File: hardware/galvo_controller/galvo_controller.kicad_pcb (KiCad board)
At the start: 2 copper layers, 116 parts, among them J1 USB_OTG, J2 Conn_01x03, J3 Conn_01x03, J4 Micro_SD_Card_Det, J5 Red, J6 White, J7 Conn_01x03, J8 Conn_01x03, Q1 DDTD113ZC, Q2 MMBT2222, Q3 MMBT2222, U1 ESP-WROOM-32D, U2 CP2104, U3 TPS54295PWP, U4 PCM3060, U5 NCP1117LP, U6 OPA2134, U7 LME49724, U8 LME49724

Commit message: Working on component placement
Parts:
- added REF**: MountingHole_3.2mm_M3_Pad, Mounting_Holes:MountingHole_3.2mm_M3_Pad, F.Cu at (233.8, 137.0)
- added REF**: MountingHole_3.2mm_M3_Pad, Mounting_Holes:MountingHole_3.2mm_M3_Pad, F.Cu at (123.4, 137.8)
- added REF**: MountingHole_3.2mm_M3_Pad, Mounting_Holes:MountingHole_3.2mm_M3_Pad, F.Cu at (138.6, 39.2)
- added REF**: MountingHole_3.2mm_M3_Pad, Mounting_Holes:MountingHole_3.2mm_M3_Pad, F.Cu at (230.8, 50.0)
- moved J7 119.4 mm to (234.4, 104.9), turned to 90 degrees
- moved J4 114.5 mm to (202.4, 139.8), turned to 180 degrees
- moved J5 105.6 mm to (233.5, 65.5), turned to 270 degrees
- moved JP2 105.5 mm to (204.4, 162.2)
- moved J8 97.8 mm to (234.4, 124.5), turned to 90 degrees
- moved C13 96.2 mm to (177.1, 58.9)
- moved C25 92.5 mm to (209.8, 158.8)
- moved J6 91.6 mm to (233.5, 84.5), turned to 270 degrees
- moved C14 90.6 mm to (177.2, 61.8)
- moved C21 90.1 mm to (214.4, 56.4), turned to 180 degrees
- moved C39 85.8 mm to (227.6, 65.6), turned to 180 degrees
- moved U4 85.7 mm to (208.2, 106.4)
- moved C2 82.5 mm to (153.2, 134.0)
- moved C41 80.4 mm to (228.8, 81.0), turned to 270 degrees
- moved C16 78.6 mm to (199.8, 118.0)
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
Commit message: Working on component placement
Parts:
- moved L1 38.7 mm to (189.5, 51.2), turned to 90 degrees
- moved REF** 37.8 mm to (161.2, 137.2)
- moved R4 35.2 mm to (185.5, 58.2), turned to 90 degrees
- moved C12 35.1 mm to (190.3, 71.6), turned to 180 degrees
- moved R3 33.4 mm to (183.7, 58.2), turned to 270 degrees
- moved C8 33.3 mm to (189.9, 59.0), turned to 180 degrees
- moved C6 31.3 mm to (190.3, 57.0)
- moved R7 29.0 mm to (157.8, 172.8)
- moved C3 29.0 mm to (166.4, 165.8)
- moved R5 29.0 mm to (163.6, 175.8)
- moved R9 29.0 mm to (157.0, 155.4)
- moved C2 29.0 mm to (171.8, 156.2)
- moved D1 29.0 mm to (163.4, 172.2)
- moved D2 29.0 mm to (157.9, 176.7)
- moved Q2 29.0 mm to (163.5, 159.2)
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
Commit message: Working on component placement
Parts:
- moved C2 52.8 mm to (119.9, 146.7)
- moved C3 52.8 mm to (114.5, 156.3)
- moved D1 52.8 mm to (111.5, 162.7)
- moved Q2 52.8 mm to (111.6, 149.7)
- moved R7 52.8 mm to (105.9, 163.3)
- moved R9 52.8 mm to (105.1, 145.9)
- moved D2 52.8 mm to (106.0, 167.2)
- moved Q3 52.8 mm to (111.8, 142.6)
- moved R10 52.8 mm to (105.3, 150.5)
- moved R5 52.8 mm to (111.7, 166.3)
- moved C10 44.9 mm to (143.0, 76.0)
- moved C11 44.9 mm to (139.8, 71.8)
- moved C12 44.9 mm to (145.8, 77.2)
- moved C13 44.9 mm to (140.0, 84.4)
- moved C14 44.9 mm to (137.4, 84.4)
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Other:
- board outline added: 80 x 100 mm

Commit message: Working on component placement
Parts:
- moved R7 52.9 mm to (125.9, 114.3)
- moved R5 52.9 mm to (131.7, 117.3)
- moved D2 52.9 mm to (126.0, 118.2)
- moved D1 52.9 mm to (131.5, 113.7)
- moved C25 19.1 mm to (181.0, 151.4)
- moved JP2 19.1 mm to (175.6, 154.8)
- moved R14 19.1 mm to (158.8, 146.4)
- moved R15 19.1 mm to (160.4, 150.4)
- moved R16 19.1 mm to (160.8, 155.4)
- moved R17 19.1 mm to (169.4, 148.6)
- moved R19 19.1 mm to (167.6, 156.6)
- moved R18 19.1 mm to (168.2, 152.6)
- moved C2 18.2 mm to (122.9, 128.7)
- moved C3 18.2 mm to (117.5, 138.3)
- moved Q2 18.2 mm to (114.6, 131.7)
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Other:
- board size 80 x 100 mm -> 75 x 90 mm

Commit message: Working on layout
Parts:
- moved C18 10.8 mm to (176.5, 58.8)
- moved C22 10.8 mm to (180.5, 65.4)
- moved U5 10.8 mm to (174.3, 64.4)
- moved C20 3.94 mm to (186.1, 85.6)
- moved C24 3.94 mm to (186.1, 89.1)
- moved C17 3.86 mm to (188.1, 85.3)
- moved C23 3.86 mm to (188.1, 89.4)
- moved U4 2.56 mm to (178.0, 88.0)
- moved C15 2.00 mm to (168.4, 88.6)
- moved C16 2.00 mm to (170.5, 88.3)
- moved D4 1.93 mm to (181.0, 70.0), turned to 0 degrees
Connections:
- net Net-(J1-Pad1) renamed /VBUS
- net Net-(J1-Pad2) renamed /D_N
- net Net-(J1-Pad3) renamed /D_P
- net Net-(J7-Pad1) renamed /X_P
- net Net-(J7-Pad2) renamed /X_N
- net Net-(J8-Pad1) renamed /Y_P
- net Net-(J8-Pad2) renamed /Y_N
- net Net-(R22-Pad1) renamed /VOUTR_N
- net Net-(R23-Pad1) renamed /VOUTR_P
- net Net-(R24-Pad1) renamed /VOUTL_N
- net Net-(R25-Pad1) renamed /VOUTL_P
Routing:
- net +3V3: track 0.00 -> 2.51 mm, vias 0 -> 1
- added copper zone on In2.Cu, net +3V3
- added copper zone on In2.Cu, net +5VD
- added copper zone on In1.Cu, net GNDA
- added copper zone on In2.Cu, net VCC
- added copper zone on In2.Cu, net VEE
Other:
- copper layers 2 -> 4
- net class Default: clearance 0.2 -> 0.1524; trace_width 0.25 -> 0.1524; via_dia 0.6 -> 0.452; via_drill 0.4 -> 0.3
- rule trace_clearance: 0.2 -> 0.1524
- rule trace_min: 0.2 -> 0.1524
- rule via_min_size: 0.4 -> 0.452

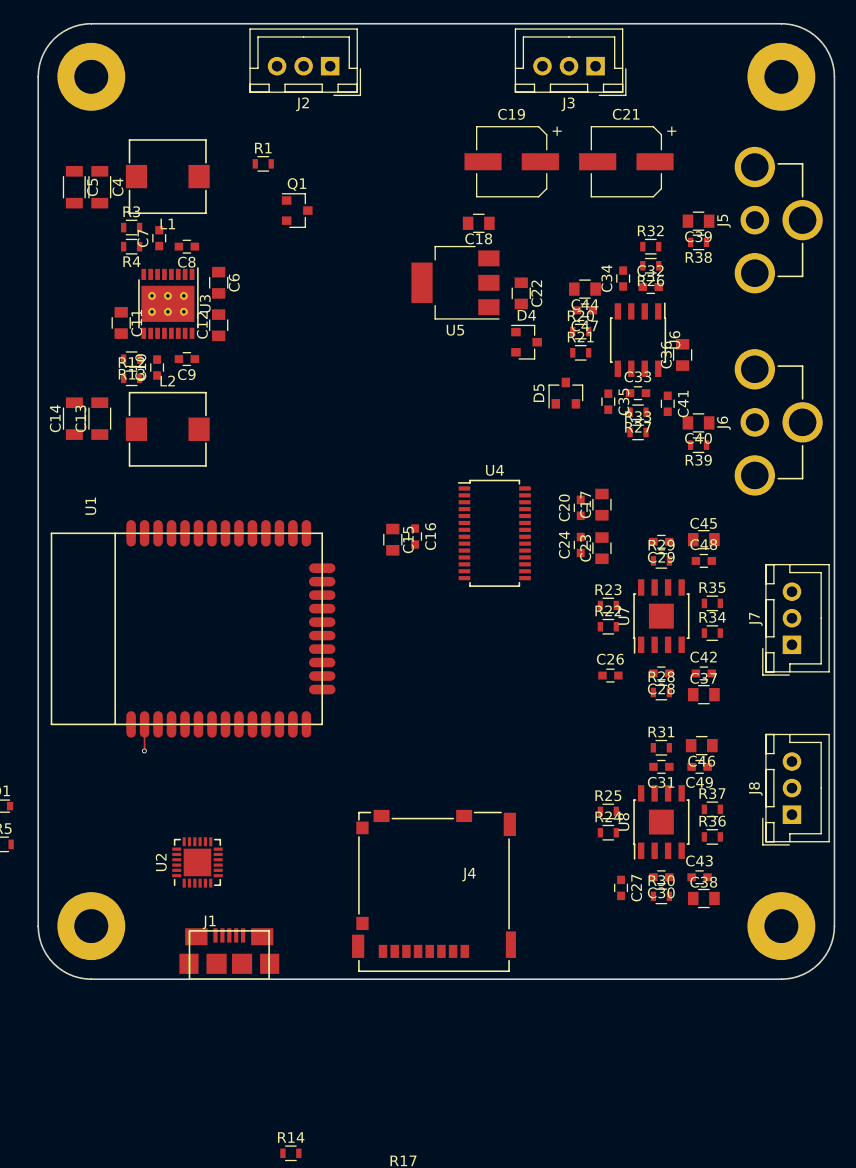
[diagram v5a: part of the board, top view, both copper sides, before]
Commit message: Switched to logic buffer for laser enable
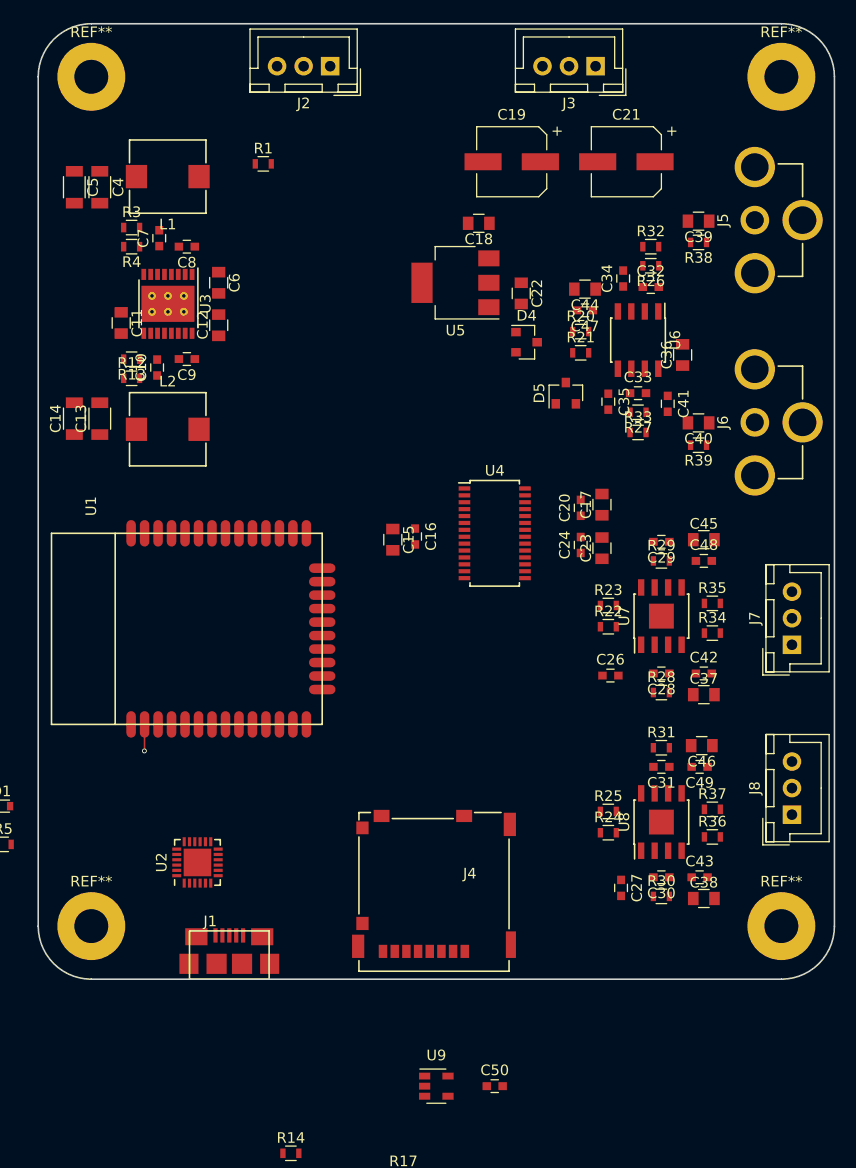
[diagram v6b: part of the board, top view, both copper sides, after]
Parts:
- removed Q1: DDTD113ZC, TO_SOT_Packages_SMD:SOT-23
- added C50: 0.1u, Capacitors_SMD:C_0603, F.Cu at (178.0, 140.1)
- added U9: SN74LV1T34, TO_SOT_Packages_SMD:SOT-23-5, F.Cu at (172.5, 140.1)
- R1: value 2.2k -> 10k
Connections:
- J4 pad 10: (no net) -> /SD_CD
- R1 pad 1: +5VD -> Net-(JP2-Pad1)
- R1 pad 2: Net-(J2-Pad3) -> /SD_CD
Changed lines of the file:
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@@
 (kicad_pcb (version 4) (host pcbnew 4.0.7)
   (general
-    (links 287)
-    (no_connects 281)
+    (links 0)
+    (no_connects 274)
     (area 134.924999 39.924999 210.075001 130.075001)
     (thickness 1.6)
@@
     (tracks 3)
     (zones 0)
-    (modules 120)
-    (nets 74)
+    (modules 121)
+    (nets 75)
   )
   (page A4)
@@
   (net 72 /D_N)
   (net 73 /D_P)
+  (net 74 /SD_CD)
   (net_class Default "This is the default net class."
     (clearance 0.1524)
@@
     (add_net /SCL)
     (add_net /SDA)
+    (add_net /SD_CD)
     (add_net /SD_CLK)
     (add_net /SD_CMD)
@@
   )
   (module Mounting_Holes:MountingHole_3.2mm_M3_Pad (layer F.Cu)
-    (at 205 125)
+    (at 140 45)
     (descr "Mounting Hole 3.2mm, M3")
     (tags "mounting hole 3.2mm m3")
     (attr virtual)
-    (fp_text reference REF** (at 0 -4.2) (layer F.SilkS) hide
+    (fp_text reference REF** (at 0 -4.2) (layer F.SilkS)
       (effects (font (size 1 1) (thickness 0.15)))
     )
@@
   )
   (module Mounting_Holes:MountingHole_3.2mm_M3_Pad (layer F.Cu)
-    (at 140 125)
+    (at 205 45)
     (descr "Mounting Hole 3.2mm, M3")
     (tags "mounting hole 3.2mm m3")
     (attr virtual)
-    (fp_text reference REF** (at 0 -4.2) (layer F.SilkS) hide
+    (fp_text reference REF** (at 0 -4.2) (layer F.SilkS)
       (effects (font (size 1 1) (thickness 0.15)))
     )
@@
   )
   (module Mounting_Holes:MountingHole_3.2mm_M3_Pad (layer F.Cu)
-    (at 140 45)
+    (at 205 125)
     (descr "Mounting Hole 3.2mm, M3")
     (tags "mounting hole 3.2mm m3")
     (attr virtual)
-    (fp_text reference REF** (at 0 -4.2) (layer F.SilkS) hide
+    (fp_text reference REF** (at 0 -4.2) (layer F.SilkS)
       (effects (font (size 1 1) (thickness 0.15)))
     )
@@
     (pad 11 smd rect (at 14.865 1.1 180) (size 1.15 2.2) (layers F.Cu F.Paste F.Mask)
       (net 50 "Net-(J4-Pad11)"))
-    (pad 10 smd rect (at 14.46 3.25 180) (size 1.16 1.25) (layers F.Cu F.Paste F.Mask))
+    (pad 10 smd rect (at 14.46 3.25 180) (size 1.16 1.25) (layers F.Cu F.Paste F.Mask)
+      (net 74 /SD_CD))
     (pad 9 smd rect (at 14.46 12.25 180) (size 1.16 1.2) (layers F.Cu F.Paste F.Mask)
       (net 1 GNDA))
@@
   )
   (module TO_SOT_Packages_SMD:SOT-23 (layer F.Cu)
-    (at 159.4 57.6)
-    (descr "SOT-23, Standard")
-    (tags SOT-23)
-    (attr smd)
-    (fp_text reference Q1 (at 0 -2.5) (layer F.SilkS)
-      (effects (font (size 1 1) (thickness 0.15)))
-    )
-    (fp_text value DDTD113ZC (at 0 2.5) (layer F.Fab)
-      (effects (font (size 1 1) (thickness 0.15)))
-    )
-    (fp_text user %R (at 0 0 90) (layer F.Fab)
-      (effects (font (size 0.5 0.5) (thickness 0.075)))
-    )
-    (fp_line (start -0.7 -0.95) (end -0.7 1.5) (layer F.Fab) (width 0.1))
-    (fp_line (start -0.15 -1.52) (end 0.7 -1.52) (layer F.Fab) (width 0.1))
-    (fp_line (start -0.7 -0.95) (end -0.15 -1.52) (layer F.Fab) (width 0.1))
-    (fp_line (start 0.7 -1.52) (end 0.7 1.52) (layer F.Fab) (width 0.1))
-    (fp_line (start -0.7 1.52) (end 0.7 1.52) (layer F.Fab) (width 0.1))
-    (fp_line (start 0.76 1.58) (end 0.76 0.65) (layer F.SilkS) (width 0.12))
-    (fp_line (start 0.76 -1.58) (end 0.76 -0.65) (layer F.SilkS) (width 0.12))
-    (fp_line (start -1.7 -1.75) (end 1.7 -1.75) (layer F.CrtYd) (width 0.05))
-    (fp_line (start 1.7 -1.75) (end 1.7 1.75) (layer F.CrtYd) (width 0.05))
-    (fp_line (start 1.7 1.75) (end -1.7 1.75) (layer F.CrtYd) (width 0.05))
-    (fp_line (start -1.7 1.75) (end -1.7 -1.75) (layer F.CrtYd) (width 0.05))
-    (fp_line (start 0.76 -1.58) (end -1.4 -1.58) (layer F.SilkS) (width 0.12))
-    (fp_line (start 0.76 1.58) (end -0.7 1.58) (layer F.SilkS) (width 0.12))
-    (pad 1 smd rect (at -1 -0.95) (size 0.9 0.8) (layers F.Cu F.Paste F.Mask))
-    (pad 2 smd rect (at -1 0.95) (size 0.9 0.8) (layers F.Cu F.Paste F.Mask)
-      (net 1 GNDA))
-    (pad 3 smd rect (at 1 0) (size 0.9 0.8) (layers F.Cu F.Paste F.Mask)
-      (net 43 "Net-(J2-Pad3)"))
-    (model ${KISYS3DMOD}/TO_SOT_Packages_SMD.3dshapes/SOT-23.wrl
-      (at (xyz 0 0 0))
-      (scale (xyz 1 1 1))
-      (rotate (xyz 0 0 0))
-    )
-  )
-  (module TO_SOT_Packages_SMD:SOT-23 (layer F.Cu)
     (at 114.6 131.7)
     (descr "SOT-23, Standard")
@@
       (effects (font (size 1 1) (thickness 0.15)))
     )
-    (fp_text value 2.2k (at 0 1.5) (layer F.Fab)
+    (fp_text value 10k (at 0 1.5) (layer F.Fab)
       (effects (font (size 1 1) (thickness 0.15)))
     )
@@
     (fp_line (start 1.25 0.7) (end -1.25 0.7) (layer F.CrtYd) (width 0.05))
     (pad 1 smd rect (at -0.75 0) (size 0.5 0.9) (layers F.Cu F.Paste F.Mask)
-      (net 5 +5VD))
+      (net 52 "Net-(JP2-Pad1)"))
     (pad 2 smd rect (at 0.75 0) (size 0.5 0.9) (layers F.Cu F.Paste F.Mask)
-      (net 43 "Net-(J2-Pad3)"))
+      (net 74 /SD_CD))
     (model ${KISYS3DMOD}/Resistors_SMD.3dshapes/R_0603.wrl
       (at (xyz 0 0 0))
@@
     )
   )
+  (module Capacitors_SMD:C_0603 (layer F.Cu)
+    (at 178 140.075001)
+    (descr "Capacitor SMD 0603, reflow soldering, AVX (see smccp.pdf)")
+    (tags "capacitor 0603")
+    (attr smd)
+    (fp_text reference C50 (at 0 -1.5) (layer F.SilkS)
+      (effects (font (size 1 1) (thickness 0.15)))
+    )
+    (fp_text value 0.1u (at 0 1.5) (layer F.Fab)
+      (effects (font (size 1 1) (thickness 0.15)))
+    )
+    (fp_line (start 1.4 0.65) (end -1.4 0.65) (layer F.CrtYd) (width 0.05))
+    (fp_line (start 1.4 0.65) (end 1.4 -0.65) (layer F.CrtYd) (width 0.05))
+    (fp_line (start -1.4 -0.65) (end -1.4 0.65) (layer F.CrtYd) (width 0.05))
+    (fp_line (start -1.4 -0.65) (end 1.4 -0.65) (layer F.CrtYd) (width 0.05))
+    (fp_line (start 0.35 0.6) (end -0.35 0.6) (layer F.SilkS) (width 0.12))
+    (fp_line (start -0.35 -0.6) (end 0.35 -0.6) (layer F.SilkS) (width 0.12))
+    (fp_line (start -0.8 -0.4) (end 0.8 -0.4) (layer F.Fab) (width 0.1))
+    (fp_line (start 0.8 -0.4) (end 0.8 0.4) (layer F.Fab) (width 0.1))
+    (fp_line (start 0.8 0.4) (end -0.8 0.4) (layer F.Fab) (width 0.1))
+    (fp_line (start -0.8 0.4) (end -0.8 -0.4) (layer F.Fab) (width 0.1))
+    (fp_text user %R (at 0 0) (layer F.Fab)
+      (effects (font (size 0.3 0.3) (thickness 0.075)))
+    )
+    (pad 2 smd rect (at 0.75 0) (size 0.8 0.75) (layers F.Cu F.Paste F.Mask)
+      (net 1 GNDA))
+    (pad 1 smd rect (at -0.75 0) (size 0.8 0.75) (layers F.Cu F.Paste F.Mask)
+      (net 5 +5VD))
+    (model Capacitors_SMD.3dshapes/C_0603.wrl
+      (at (xyz 0 0 0))
+      (scale (xyz 1 1 1))
+      (rotate (xyz 0 0 0))
+    )
+  )
+  (module TO_SOT_Packages_SMD:SOT-23-5 (layer F.Cu)
+    (at 172.5 140.075001)
+    (descr "5-pin SOT23 package")
+    (tags SOT-23-5)
+    (attr smd)
+    (fp_text reference U9 (at 0 -2.9) (layer F.SilkS)
+      (effects (font (size 1 1) (thickness 0.15)))
+    )
+    (fp_text value SN74LV1T34 (at 0 2.9) (layer F.Fab)
+      (effects (font (size 1 1) (thickness 0.15)))
+    )
+    (fp_text user %R (at 0 0 90) (layer F.Fab)
+      (effects (font (size 0.5 0.5) (thickness 0.075)))
+    )
+    (fp_line (start -0.9 1.61) (end 0.9 1.61) (layer F.SilkS) (width 0.12))
+    (fp_line (start 0.9 -1.61) (end -1.55 -1.61) (layer F.SilkS) (width 0.12))
+    (fp_line (start -1.9 -1.8) (end 1.9 -1.8) (layer F.CrtYd) (width 0.05))
+    (fp_line (start 1.9 -1.8) (end 1.9 1.8) (layer F.CrtYd) (width 0.05))
+    (fp_line (start 1.9 1.8) (end -1.9 1.8) (layer F.CrtYd) (width 0.05))
+    (fp_line (start -1.9 1.8) (end -1.9 -1.8) (layer F.CrtYd) (width 0.05))
+    (fp_line (start -0.9 -0.9) (end -0.25 -1.55) (layer F.Fab) (width 0.1))
+    (fp_line (start 0.9 -1.55) (end -0.25 -1.55) (layer F.Fab) (width 0.1))
+    (fp_line (start -0.9 -0.9) (end -0.9 1.55) (layer F.Fab) (width 0.1))
+    (fp_line (start 0.9 1.55) (end -0.9 1.55) (layer F.Fab) (width 0.1))
+    (fp_line (start 0.9 -1.55) (end 0.9 1.55) (layer F.Fab) (width 0.1))
+    (pad 1 smd rect (at -1.1 -0.95) (size 1.06 0.65) (layers F.Cu F.Paste F.Mask))
+    (pad 2 smd rect (at -1.1 0) (size 1.06 0.65) (layers F.Cu F.Paste F.Mask))
+    (pad 3 smd rect (at -1.1 0.95) (size 1.06 0.65) (layers F.Cu F.Paste F.Mask)
+      (net 1 GNDA))
+    (pad 4 smd rect (at 1.1 0.95) (size 1.06 0.65) (layers F.Cu F.Paste F.Mask)
+      (net 43 "Net-(J2-Pad3)"))
+    (pad 5 smd rect (at 1.1 -0.95) (size 1.06 0.65) (layers F.Cu F.Paste F.Mask)
+      (net 5 +5VD))
+    (model ${KISYS3DMOD}/TO_SOT_Packages_SMD.3dshapes/SOT-23-5.wrl
+      (at (xyz 0 0 0))
+      (scale (xyz 1 1 1))
+      (rotate (xyz 0 0 0))
+    )
+  )
   (module Mounting_Holes:MountingHole_3.2mm_M3_Pad (layer F.Cu)
-    (at 205 45)
+    (at 140 125)
     (descr "Mounting Hole 3.2mm, M3")
     (tags "mounting hole 3.2mm m3")
     (attr virtual)
-    (fp_text reference REF** (at 0 -4.2) (layer F.SilkS) hide
+    (fp_text reference REF** (at 0 -4.2) (layer F.SilkS)
       (effects (font (size 1 1) (thickness 0.15)))
     )
@@
         (xy 134 39) (xy 168 39) (xy 168 65.5) (xy 169 65.5) (xy 169 39)
         (xy 211 39) (xy 211 131) (xy 183 131) (xy 183 110) (xy 178 110)
-        (xy 178 78) (xy 169 78) (xy 169 66.5) (xy 168 66.5) (xy 168 79)
+        (xy 178 78) (xy 169 78) (xy 169 67) (xy 168 67) (xy 168 79)
         (xy 177 79) (xy 177 111) (xy 182 111) (xy 182 131) (xy 134 131)
       )

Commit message: Working on layout
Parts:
- moved C1 111.5 mm to (156.0, 30.8), turned to 270 degrees
- moved U1 110.1 mm to (158.8, 30.8), turned to 90 degrees
- moved R19 90.1 mm to (174.0, 141.5)
- moved C11 7.60 mm to (153.8, 72.4)
- moved C10 7.60 mm to (156.6, 71.6)
- moved L1 7.60 mm to (154.8, 54.4)
- moved L2 7.60 mm to (154.8, 78.2)
- moved U4 7.60 mm to (154.8, 66.4)
- moved C13 7.60 mm to (159.6, 68.4)
- moved C14 7.60 mm to (148.4, 77.2)
- moved C15 7.60 mm to (146.0, 77.2)
- moved C5 7.60 mm to (148.4, 55.4)
- moved C6 7.60 mm to (146.0, 55.4)
- moved C7 7.60 mm to (159.6, 64.4)
- moved C8 7.60 mm to (154.0, 60.2)
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- renumbered C50 to C1, C9 to C10, C10 to C11, C11 to C12, C12 to C13, C13 to C14, C14 to C15, C15 to C16, C16 to C17, C17 to C18, C18 to C19, C1 to C2, C19 to C20, C20 to C21, C21 to C22, C22 to C23, C23 to C24, C24 to C25, C25 to C26, C26 to C27, C27 to C28, C28 to C29, C2 to C3, C29 to C30, C30 to C31, C31 to C32, C32 to C33, C33 to C34, C34 to C35, C35 to C36, C36 to C37, C37 to C38, C38 to C39, C3 to C4, C39 to C40, C40 to C41, C41 to C42, C42 to C43, C43 to C44, C44 to C45, C45 to C46, C46 to C47, C47 to C48, C48 to C49, C4 to C5, C49 to C50, C5 to C6, C6 to C7, C7 to C8, C8 to C9, Q2 to Q1, Q3 to Q2, R2 to R1, R11 to R10, R12 to R11, R13 to R12, R14 to R13, R15 to R14, R16 to R15, R17 to R16, R18 to R17, R19 to R18, R1 to R19, R3 to R2, R4 to R3, R5 to R4, R6 to R5, R7 to R6, R8 to R7, R9 to R8, R10 to R9, U9 to U1, U1 to U2, U2 to U3, U3 to U4, U4 to U5, U5 to U6, U6 to U7, U7 to U8, U8 to U9
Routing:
- net +3V3: track 2.51 -> 3.04 mm
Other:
- board size 75 x 90 mm -> 70 x 90 mm

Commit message: Tweaked SD card pullup jumpers
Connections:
- R14 pad 1: Net-(JP2-Pad1) -> +3V3
- R15 pad 1: Net-(JP2-Pad1) -> +3V3
- R16 pad 1: Net-(JP2-Pad1) -> +3V3
- R18 pad 1: Net-(JP2-Pad1) -> +3V3
- R19 pad 1: Net-(JP2-Pad1) -> +3V3
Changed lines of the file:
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@@
     (links 290)
     (no_connects 274)
-    (area 134.924999 39.924999 210.075001 130.075001)
+    (area 139.924999 39.924999 210.075001 130.075001)
     (thickness 1.6)
     (drawings 8)
@@
     (fp_line (start 1.25 0.7) (end -1.25 0.7) (layer F.CrtYd) (width 0.05))
     (pad 1 smd rect (at -0.75 0) (size 0.5 0.9) (layers F.Cu F.Paste F.Mask)
-      (net 45 "Net-(JP2-Pad1)"))
+      (net 3 +3V3))
     (pad 2 smd rect (at 0.75 0) (size 0.5 0.9) (layers F.Cu F.Paste F.Mask)
       (net 64 /SD_CD))
@@
     (fp_line (start 1.25 0.7) (end -1.25 0.7) (layer F.CrtYd) (width 0.05))
     (pad 1 smd rect (at -0.75 0) (size 0.5 0.9) (layers F.Cu F.Paste F.Mask)
-      (net 45 "Net-(JP2-Pad1)"))
+      (net 3 +3V3))
     (pad 2 smd rect (at 0.75 0) (size 0.5 0.9) (layers F.Cu F.Paste F.Mask)
       (net 38 /SD_DAT3))
@@
     (fp_line (start 1.25 0.7) (end -1.25 0.7) (layer F.CrtYd) (width 0.05))
     (pad 1 smd rect (at -0.75 0) (size 0.5 0.9) (layers F.Cu F.Paste F.Mask)
-      (net 45 "Net-(JP2-Pad1)"))
+      (net 3 +3V3))
     (pad 2 smd rect (at 0.75 0) (size 0.5 0.9) (layers F.Cu F.Paste F.Mask)
       (net 39 /SD_CMD))
@@
     (fp_line (start 1.25 0.7) (end -1.25 0.7) (layer F.CrtYd) (width 0.05))
     (pad 1 smd rect (at -0.75 0) (size 0.5 0.9) (layers F.Cu F.Paste F.Mask)
-      (net 45 "Net-(JP2-Pad1)"))
+      (net 3 +3V3))
     (pad 2 smd rect (at 0.75 0) (size 0.5 0.9) (layers F.Cu F.Paste F.Mask)
       (net 40 /SD_CLK))
@@
     (fp_line (start 1.25 0.7) (end -1.25 0.7) (layer F.CrtYd) (width 0.05))
     (pad 1 smd rect (at -0.75 0) (size 0.5 0.9) (layers F.Cu F.Paste F.Mask)
-      (net 45 "Net-(JP2-Pad1)"))
+      (net 3 +3V3))
     (pad 2 smd rect (at 0.75 0) (size 0.5 0.9) (layers F.Cu F.Paste F.Mask)
       (net 42 /SD_DAT1))
@@
   (gr_line (start 210 125) (end 210 45) (layer Edge.Cuts) (width 0.15))
   (gr_line (start 145 130) (end 205 130) (layer Edge.Cuts) (width 0.15))
+  (segment (start 145.02 108.48) (end 145 108.5) (width 0.1524) (layer F.Cu) (net 0))
   (segment (start 151.02 106) (end 151.02 103.02) (width 0.1524) (layer F.Cu) (net 3))
   (segment (start 151.02 103.02) (end 151 103) (width 0.1524) (layer F.Cu) (net 3))
   (via (at 151 103) (size 0.452) (drill 0.3) (layers F.Cu B.Cu) (net 3))
-  (segment (start 145.02 108.48) (end 145 108.5) (width 0.1524) (layer F.Cu) (net 3))
   (zone (net 1) (net_name GNDA) (layer In1.Cu) (hatch edge 0.508)
     (connect_pads (clearance 0.16))
